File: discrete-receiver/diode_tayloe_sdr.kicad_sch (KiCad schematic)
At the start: 7 parts, among them J2 Optional 5V DC Jack, J3 USB_C_Receptacle_USB2.0_16P, J4 RJ45_Hanrun_HR911105A_Horizon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, U9 LAN8720A

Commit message: update schematic for peter
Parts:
- removed J4: RJ45_Hanrun_HR911105A_Horizontal, Connector_RJ:RJ45_Hanrun_HR911105A_Horizontal, symbol Connector:RJ45_Hanrun_HR911105A_Horizontal
- removed U9: LAN8720A, Package_DFN_QFN:VQFN-24-1EP_4x4mm_P0.5mm_EP2.5x2.5mm_ThermalVias, symbol Interface_Ethernet:LAN8720A
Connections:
- net Pico_USB_D+ renamed Pico/Pico_USB-
- net Pico_USB_D- renamed Pico/Pico_USB+
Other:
- sheet SDR_ADC renamed ADC
- added sheet Ethernet Interface (ethernet_interface.kicad_sch)
- sheet ADC: file sdr_adc.kicad_sch -> adc.kicad_sch
- sheet Pico ports: added Pico_USB+, Pico_USB-; removed none
- sheet Receiver ports: added I_CLK, I_out, LO_VFO, Q_CLK, Q_out; removed none
- moved on the sheet: D2, J2, J3, R14, R15

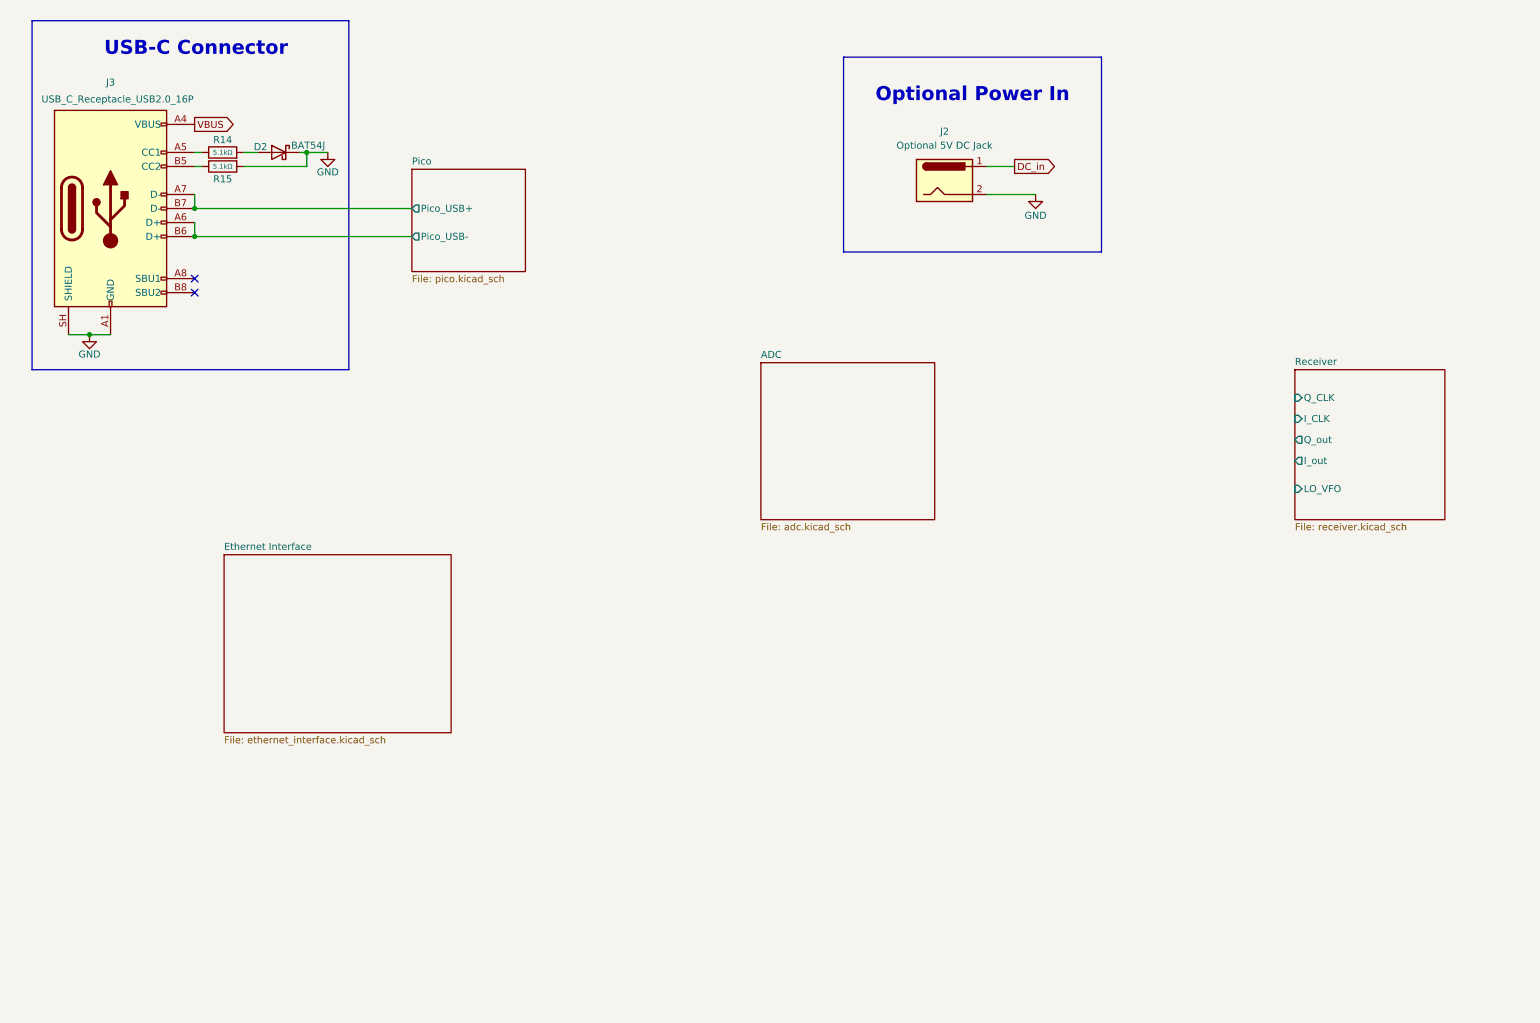
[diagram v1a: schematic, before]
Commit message: updated schematic
clock generator, ADC, and 24.576 oscillator
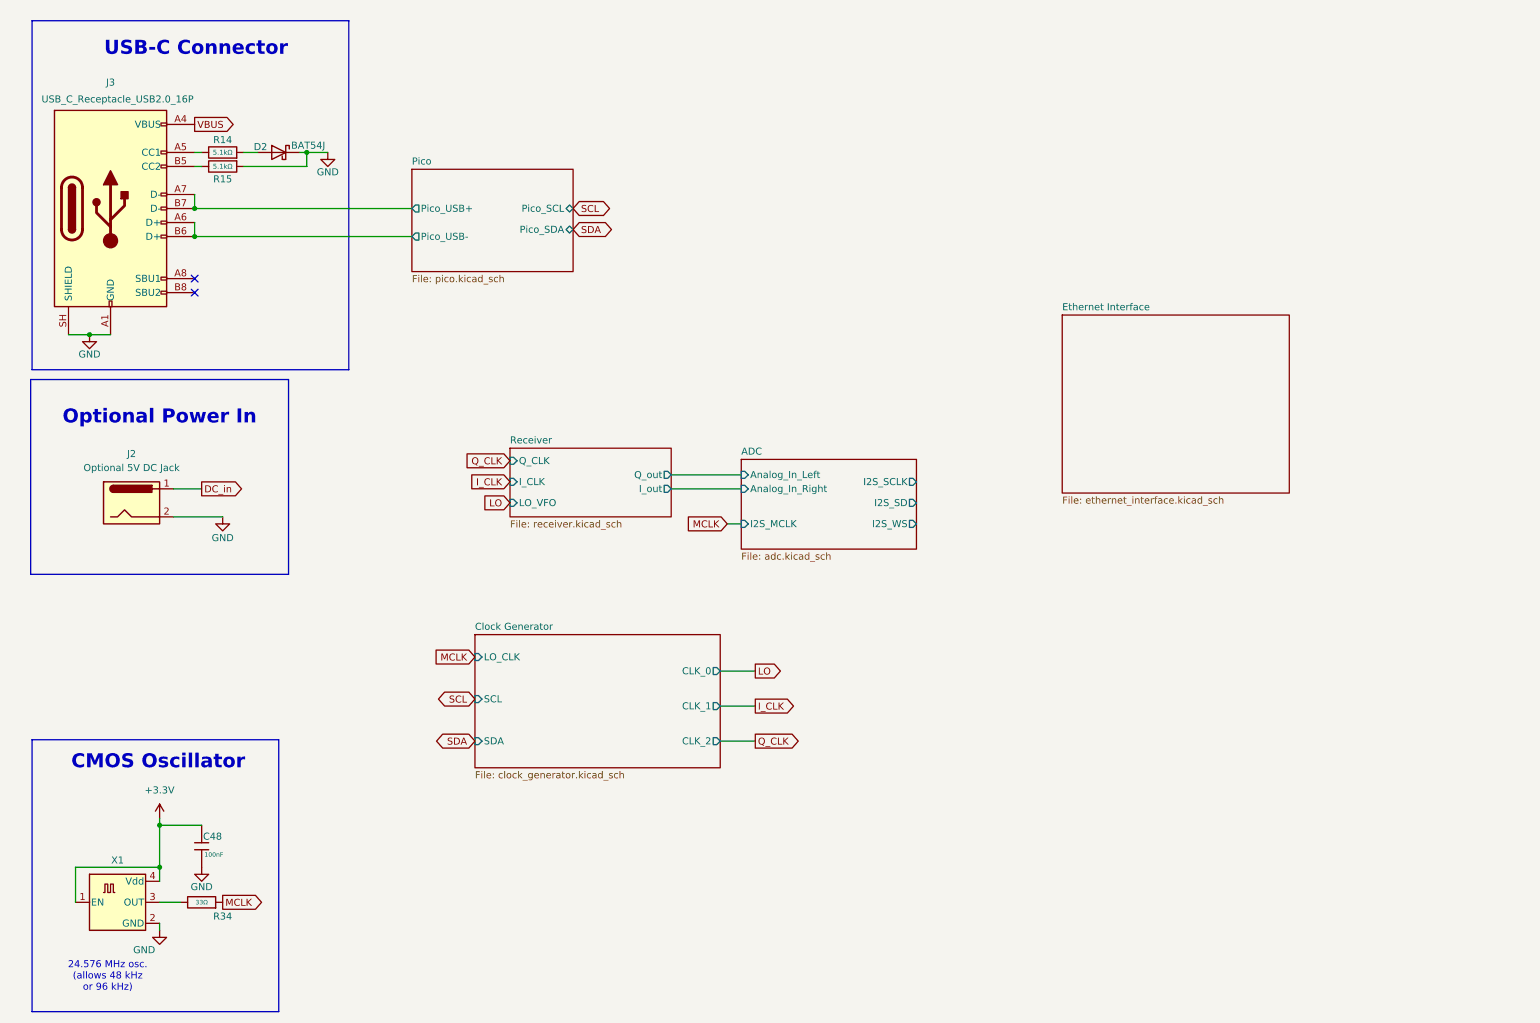
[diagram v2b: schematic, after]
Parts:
- added C48: 100nF, PCM_JLCPCB:C_0805, symbol PCM_JLCPCB-Capacitors:0805,100nF
- added R34: 33Ω, PCM_JLCPCB:R_0805, symbol PCM_JLCPCB-Resistors:0805,33Ω
- added X1: YC24.576MUBCE2O, Oscillator:Oscillator_SMD_Abracon_ASE-4Pin_3.2x2.5mm, symbol Oscillator:ASE-xxxMHz
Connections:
- net GND: now also C48.2, X1.2 (GND)
- new net: R34.2, X1.3 (OUT)
- new net +3.3V: C48.1, X1.1 (EN), X1.4 (Vdd)
- new net MCLK: R34.1
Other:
- added sheet Clock Generator (clock_generator.kicad_sch)
- sheet ADC ports: added Analog_In_Left, Analog_In_Right, I2S_MCLK, I2S_SCLK, I2S_SD, I2S_WS; removed none
- sheet Pico ports: added Pico_SCL, Pico_SDA; removed none
- note added: "24.576 MHz osc. (allows 48 kHz or 96 kHz)"
- note added: "CMOS Oscillator"
- moved on the sheet: J2

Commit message: POE implemented, working on finishing Ethernet Implementation
I've added the SI-52003 rj45 jack with included magnetics, which is designed for POE and has outputs for such. The 4 power lines pass through two full bridge rectifiers to ensure the polarity of a 48V POE source, then that voltage is fed to an AG9905LP DC-DC converter. This module is designed to be low-noise, although still not perfect. By jumpering its ADJ pin to V- (GND), we can boost it's output voltage to 5.65V rather than 5V. Then, we can use a low-noise LDO regulator to filter the voltage as much as possible to create a good 5V source for the rest of the components on the board. Three LM66100 ICs are used as ideal diodes to select whichever of the three power sources has the highest voltage, and not allow backfeeding into the others. These three 5V power sources are USB, barrel jack, and POE. At this point all power sources pass through the TPS7A20, which is our 5V low-noise LDO regulator. That gives us the main 5V bus.
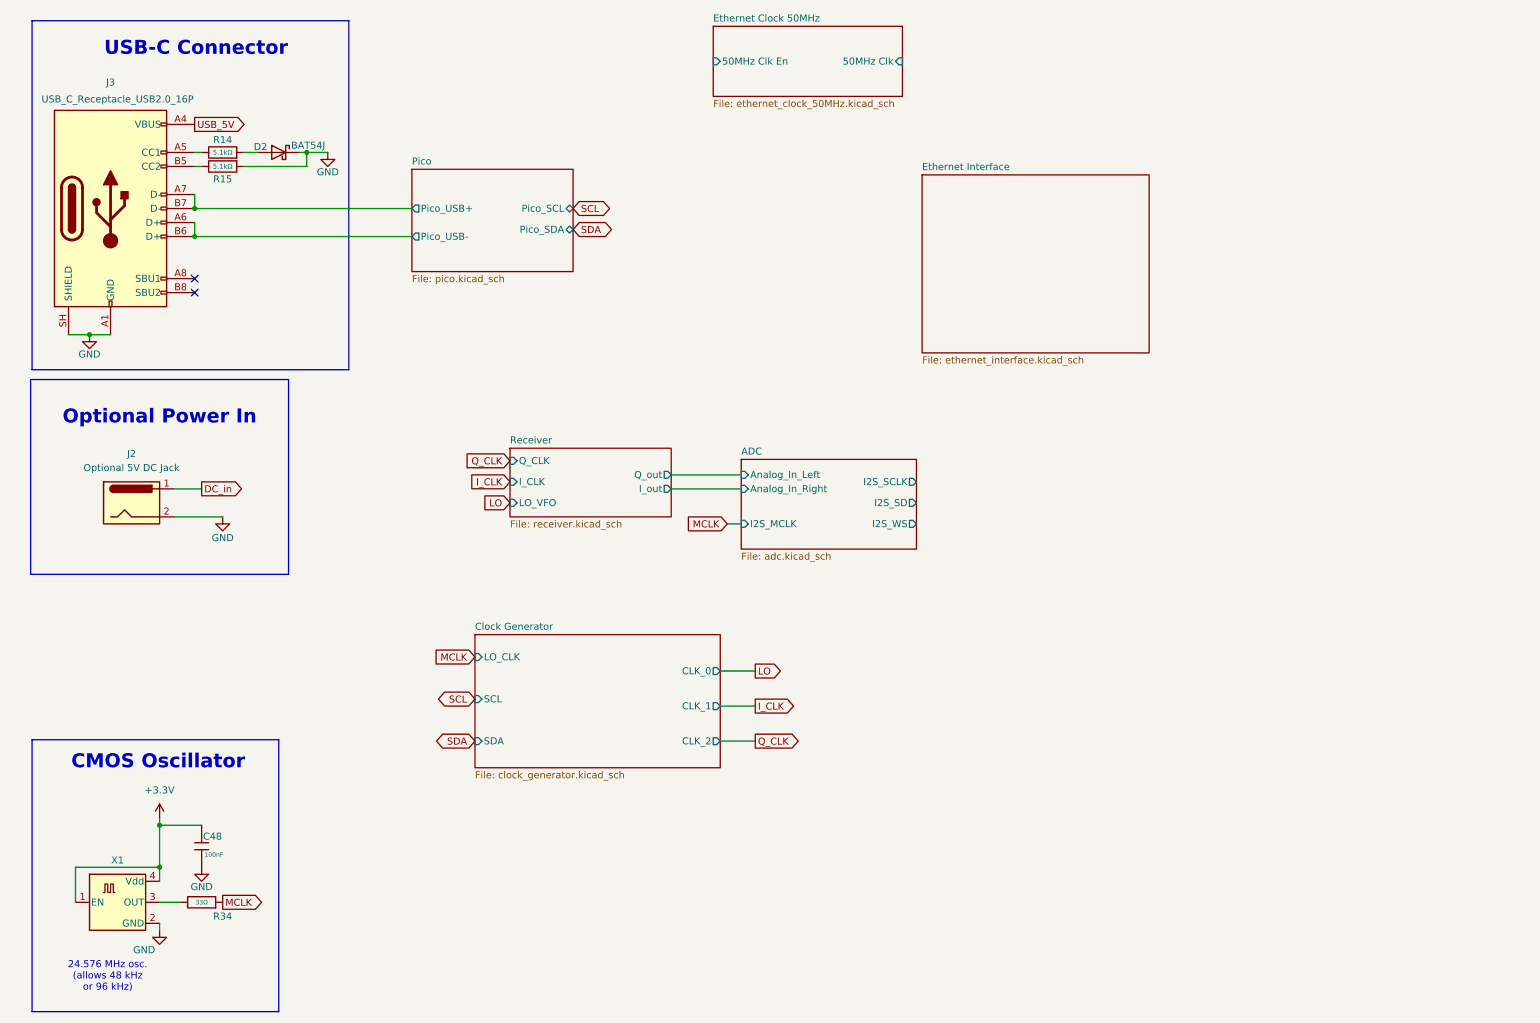
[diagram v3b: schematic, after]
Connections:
- net VBUS renamed USB_5V
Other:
- added sheet Ethernet Clock 50MHz (ethernet_clock_50MHz.kicad_sch)
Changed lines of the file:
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@@
 		)
 	)
-	(global_label "VBUS"
+	(global_label "USB_5V"
 		(shape output)
 		(at 44.45 34.29 0)
@@
 		)
 		(property "Intersheetrefs" "${INTERSHEET_REFS}"
-			(at 52.3338 34.29 0)
+			(at 54.5109 34.29 0)
 			(hide yes)
 			(show_name no)
@@
 	)
 	(sheet
-		(at 201.676 68.834)
+		(at 176.276 43.434)
 		(size 41.148 32.258)
 		(exclude_from_sim no)
@@
 		)
 		(property "Sheetname" "Ethernet Interface"
-			(at 201.676 68.1224 0)
+			(at 176.276 42.7224 0)
 			(show_name no)
 			(do_not_autoplace no)
@@
 		)
 		(property "Sheetfile" "ethernet_interface.kicad_sch"
-			(at 201.676 101.6766 0)
+			(at 176.276 76.2766 0)
 			(show_name no)
 			(do_not_autoplace no)
@@
 				)
 			)
+		)
+	)
+	(sheet
+		(at 138.43 16.51)
+		(size 34.29 12.7)
+		(exclude_from_sim no)
+		(in_bom yes)
+		(on_board yes)
+		(dnp no)
+		(fields_autoplaced yes)
+		(stroke
+			(width 0.1524)
+			(type solid)
+		)
+		(fill
+			(color 0 0 0 0)
+		)
+		(property "Sheetname" "Ethernet Clock 50MHz"
+			(at 138.43 15.7984 0)
+			(show_name no)
+			(do_not_autoplace no)
+			(effects
+				(font
+					(size 1.27 1.27)
+				)
+				(justify left bottom)
+			)
+		)
+		(property "Sheetfile" "ethernet_clock_50MHz.kicad_sch"
+			(at 138.43 29.7946 0)
+			(show_name no)
+			(do_not_autoplace no)
+			(effects
+				(font
+					(size 1.27 1.27)
+				)
+				(justify left top)
+			)
+		)
+		(pin "50MHz Clk" input
+			(at 172.72 22.86 0)
+			(effects
+				(font
+					(size 1.27 1.27)
+				)
+				(justify right)
+			)
+		)
+		(pin "50MHz Clk En" input
+			(at 138.43 22.86 180)
+			(effects
+				(font
+					(size 1.27 1.27)
+				)
+				(justify left)
+			)
+		)
+		(instances
+			(project "diode_tayloe_sdr"
+				(path "/d18d178d-3f10-4d68-9036-eae71a7d091a"
+					(page "7")
+				)
+			)

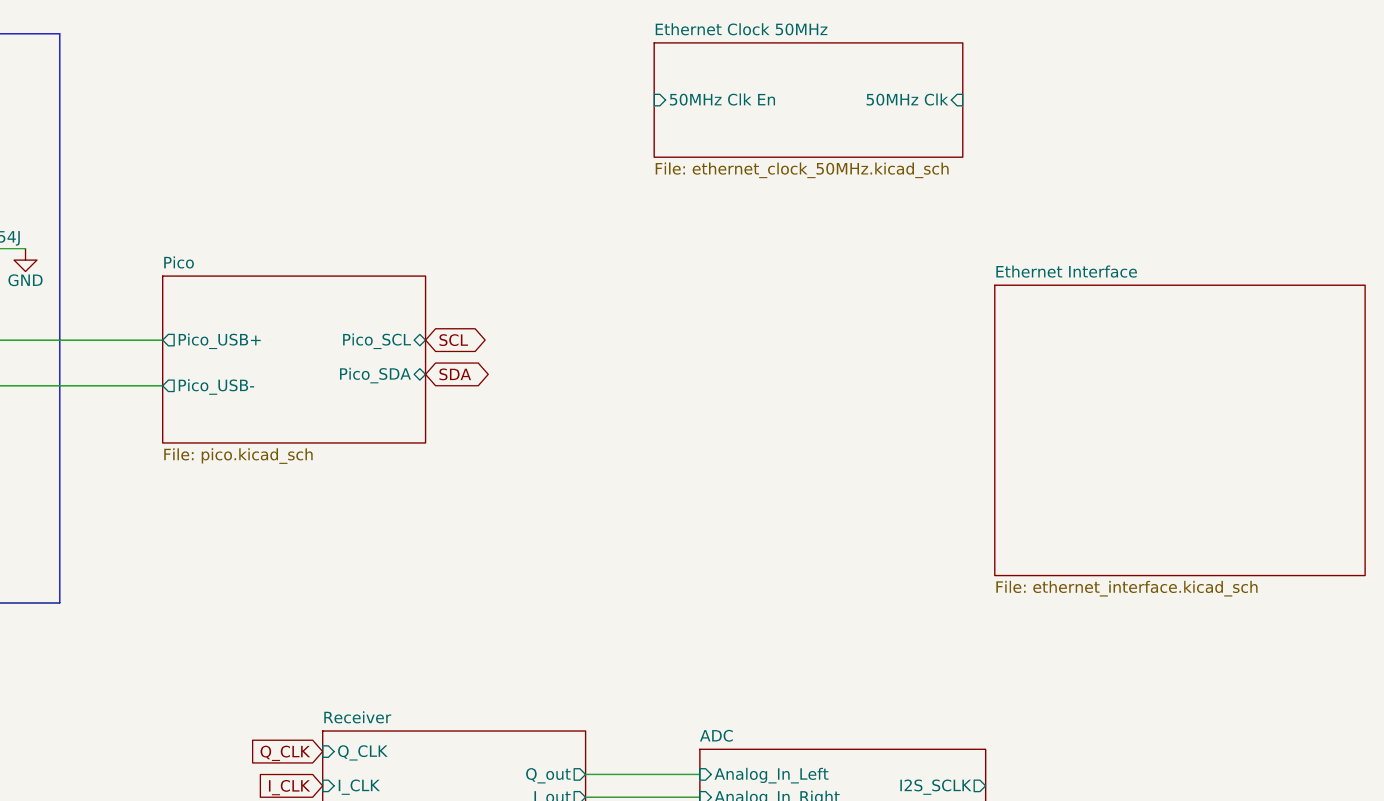
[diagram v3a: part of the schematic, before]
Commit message: Finished Ethernet Hardware Implementation
Ethernet is now implemented using the LAN8720a IC as well as the RP2350's PIO blocks to hopefully support full speed transfer of 192kHz 24 bit stereo audio, as well as control and maybe even a web interface.
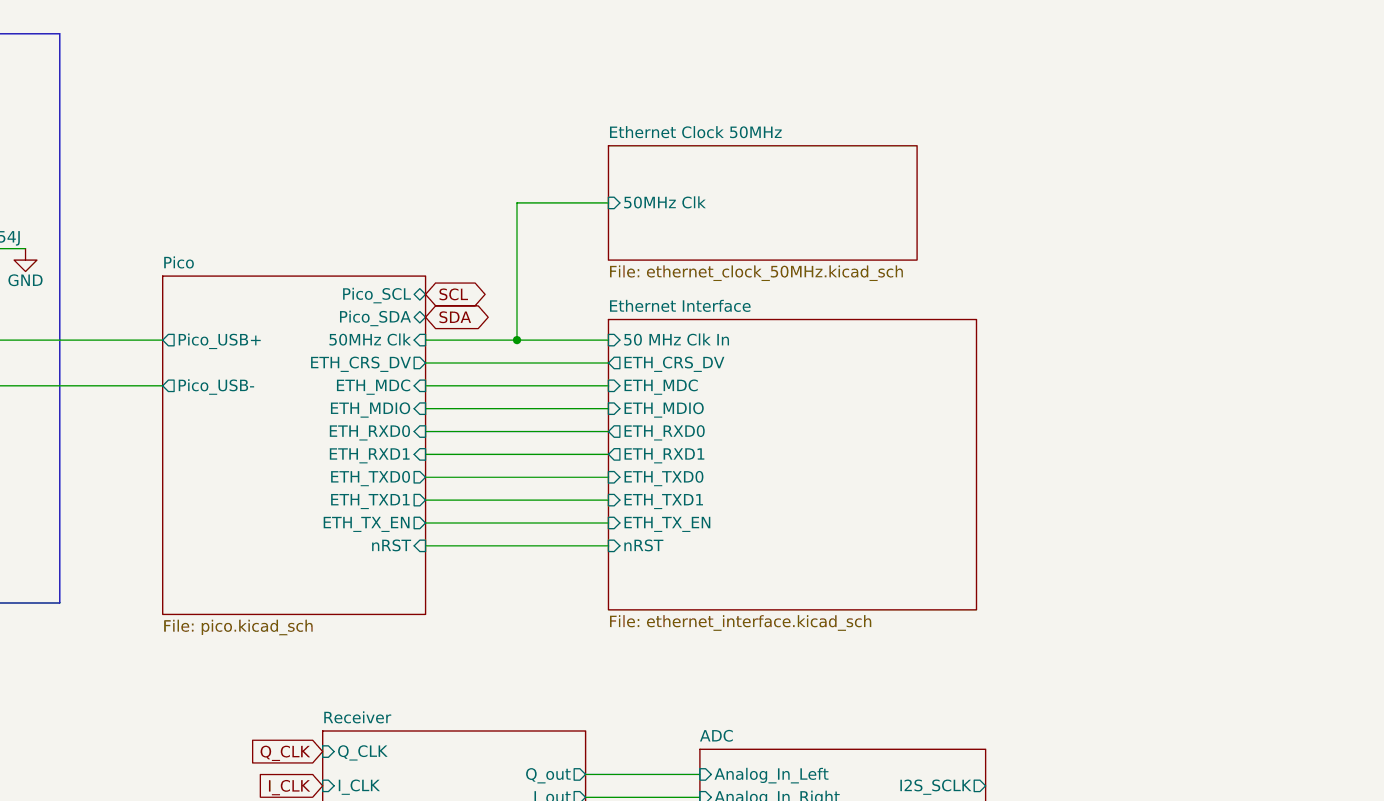
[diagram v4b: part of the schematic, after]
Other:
- sheet Ethernet Clock 50MHz ports: added none; removed 50MHz Clk En
- sheet Ethernet Interface ports: added 50 MHz Clk In, ETH_CRS_DV, ETH_MDC, ETH_MDIO, ETH_RXD0, ETH_RXD1, ETH_TXD0, ETH_TXD1, ETH_TX_EN, nRST; removed none
- sheet Pico ports: added 50MHz Clk, ETH_CRS_DV, ETH_MDC, ETH_MDIO, ETH_RXD0, ETH_RXD1, ETH_TXD0, ETH_TXD1, ETH_TX_EN, nRST; removed none

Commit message: Fixed a couple bugs
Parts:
- removed D2: BAT54J, Diode_SMD:D_SOD-323F, symbol Diode:BAT54J
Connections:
- net GND: now also R14.2
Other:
- sheet Ethernet Interface ports: added 50 MHz Clk; removed 50 MHz Clk In
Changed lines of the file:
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@@
-	(wire
-		(pts
-			(xy 63.5 39.37) (xy 64.77 39.37)
-		)
-		(stroke
-			(width 0)
-			(type default)
-		)
-	)
 	(wire
 		(pts
@@
 	(wire
 		(pts
-			(xy 55.88 39.37) (xy 53.34 39.37)
+			(xy 53.34 39.37) (xy 64.77 39.37)
 		)
 		(stroke
@@
 				)
 				(justify right)
-			)
-		)
-	)
-	(symbol
-		(lib_id "Diode:BAT54J")
-		(at 59.69 39.37 0)
-		(mirror y)
-		(unit 1)
-		(body_style 1)
-		(exclude_from_sim no)
-		(in_bom yes)
-		(on_board yes)
-		(in_pos_files yes)
-		(dnp no)
-		(property "Reference" "D2"
-			(at 56.388 38.354 0)
-			(show_name no)
-			(do_not_autoplace no)
-			(effects
-				(font
-					(size 1.27 1.27)
-				)
-			)
-		)
-		(property "Value" "BAT54J"
-			(at 65.024 38.1 0)
-			(show_name no)
-			(do_not_autoplace no)
-			(effects
-				(font
-					(size 1.27 1.27)
-				)
-			)
-		)
-		(property "Footprint" "Diode_SMD:D_SOD-323F"
-			(at 59.69 43.815 0)
-			(hide yes)
-			(show_name no)
-			(do_not_autoplace no)
-			(effects
-				(font
-					(size 1.27 1.27)
-				)
-			)
-		)
-		(property "Datasheet" "https://assets.nexperia.com/documents/data-sheet/BAT54J.pdf"
-			(at 59.69 39.37 0)
-			(hide yes)
-			(show_name no)
-			(do_not_autoplace no)
-			(effects
-				(font
-					(size 1.27 1.27)
-				)
-			)
-		)
-		(property "Description" "30V 200mA Schottky diode, SOD-323F"
-			(at 59.69 39.37 0)
-			(hide yes)
-			(show_name no)
-			(do_not_autoplace no)
-			(effects
-				(font
-					(size 1.27 1.27)
-				)
-			)
-		)
-		(pin "2"
-		)
-		(pin "1"
-		)
-		(instances
-			(project "diode_tayloe_sdr"
-				(path "/d18d178d-3f10-4d68-9036-eae71a7d091a"
-					(reference "D2")
-					(unit 1)
-				)
 			)
 		)
@@
 			)
 		)
-		(pin "50 MHz Clk In" input
+		(pin "50 MHz Clk" input
 			(at 133.35 49.53 180)
 			(effects
